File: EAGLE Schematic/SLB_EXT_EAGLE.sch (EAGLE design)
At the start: 706 parts, among them J1 16P_HEADER_SMD, J10 DB2EVC-3.81-4P-GN, J11 1803280, J12 KH-PCB-6P6C, J13 WJ15EDGK-3.81-2P, J14 KH-PCB-6P6C, J15 B4B-XH-A(LF)(SN), J17 WJ15EDGK-3.81-2P, J18 B3B-XH-A(LF)(SN), J19 DNI, J2 Phoenix Pluggable 3.81mm 3 way, J20 USB-C-Socket, J21 B3B-XH-A(LF)(SN), J3 Phoenix Pluggable 3.81mm 2 way, J4 B4B-XH-A(LF)(SN), J5 B4B-XH-A(LF)(SN), J6 B4B-XH-A(LF)(SN), J7 B4B-XH-A(LF)(SN), J8 B4B-XH-A(LF)(SN), J9 1803455, K1_TR1 TLP3109A, K1_TR2 TLP3109A, K2 VCF4-1000, P1 DB2EVC-3.81-2P-GN, P10 DB2ERC-5.08-2P-GN, P11 SHROUDED_BOX_HEADER_40, P12 HR911105A, P13 SHROUDED_BOX_HEADER_08, P14 SHROUDED_BOX_HEADER_08, P15 DNI, P16 SHROUDED_BOX_HEADER_08, P17 DB2EVC-3.81-7P-GN, P18_RL1 WJ15EDGK-3.81-2P, P18_RL2 WJ15EDGK-3.81-2P, P19 WJ15EDGK-3.81-2P, P2 DB2EVC-3.81-2P-GN, P20 SHROUDED_BOX_HEADER_08, P21_TR1 WJ15EDGK-3.81-2P, P21_TR2 WJ15EDGK-3.81-2P, P23 22284020, P24 1803329, P25 DNI, P26 DNI, P27 SHROUDED_BOX_HEADER_08, P28 DB2EVC-3.81-2P-GN, P3 DB2EVC-3.81-2P-GN, P4 DB2EVC-3.81-2P-GN, P5 Header 2, P6 WJ15EDGK-3.81-2P, P8 DNI, P9 DNI, Q1 WSF50P10, Q10_RL1 2N7002-7-F, Q10_RL2 2N7002-7-F, Q11 2N7002-7-F, Q12 2N7002-7-F, Q13 ST3422A, Q14 CSD19538Q3A, Q15 CSD19538Q3A, Q16 BSS123, Q17 BSS123, Q2_RL1 ST3422A, Q2_RL2 ST3422A, Q3 2N7002-7-F, Q4 2N7002-7-F, Q5 2N7002-7-F, Q6 2N7002-7-F, Q7 2N7002-7-F, Q8 2N7002-7-F, Q9_TR1 2N7002-7-F, Q9_TR2 2N7002-7-F, U1 SN74AHC1G86DBVR, U10 EL357N-G, U11 W5500, U12 CBMUD1201LAS8, U13 SN75176BDR, U14 ADUM1200ARZ-RL7, U15 EL357N-G, U16 TPS54331DR, U17 STM32F412VGT6STM32F412VGT6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

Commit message: Updated schematic
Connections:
- net HALT_PEN: now also U21.C
- net KPSTR_PEN: now also U22.C
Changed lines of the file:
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@@
 <label x="342.9" y="142.24" size="1.778" layer="95" rot="MR0"/>
+</segment>
+<segment>
+<pinref part="U21" gate="G$1" pin="C"/>
+<wire x1="124.46" y1="76.2" x2="142.24" y2="76.2" width="0.1524" layer="91"/>
+<label x="129.54" y="76.2" size="1.778" layer="95"/>
 </segment>
 </net>
@@
 <label x="342.9" y="139.7" size="1.778" layer="95" rot="MR0"/>
 </segment>
+<segment>
+<pinref part="U22" gate="G$1" pin="C"/>
+<wire x1="124.46" y1="38.1" x2="140.97" y2="38.1" width="0.1524" layer="91"/>
+<label x="127" y="38.1" size="1.778" layer="95"/>
+</segment>
 </net>

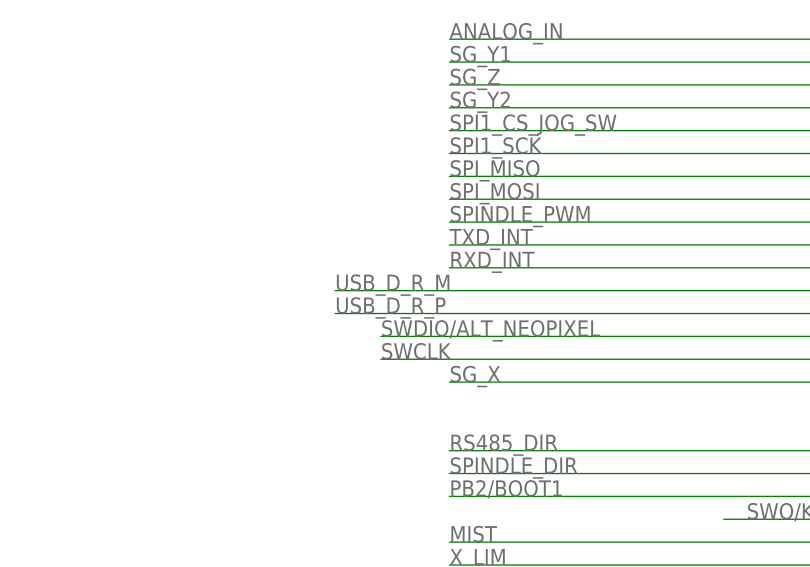
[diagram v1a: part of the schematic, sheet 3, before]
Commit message: Updated schematic (Incorrectly named NET)
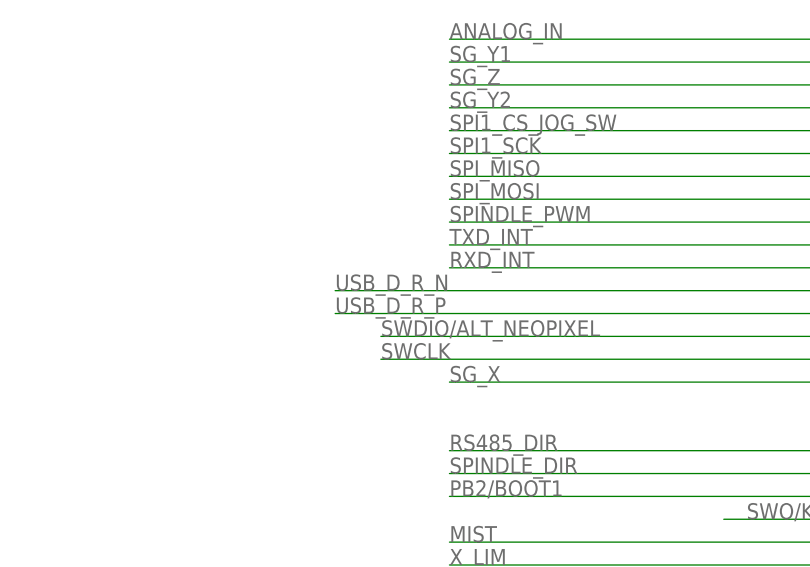
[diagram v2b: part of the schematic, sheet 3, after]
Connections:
- removed net USB_D_R_M: U17.PA11/OTG_FS_DM
- net USB_D_R_N: now also U17.PA11/OTG_FS_DM
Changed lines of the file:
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@@
 </busses>
 <nets>
-<net name="USB_D_R_M" class="0">
-<segment>
-<wire x1="132.08" y1="104.14" x2="76.2" y2="104.14" width="0.1524" layer="91"/>
-<label x="76.2" y="104.14" size="1.778" layer="95"/>
-<pinref part="U17" gate="G$1" pin="PA11/OTG_FS_DM"/>
-</segment>
-</net>
 <net name="STM_NRST" class="0">
 <segment>
@@
 <pinref part="R67" gate="G$1" pin="1"/>
 </segment>
-</net>
+<segment>
+<wire x1="132.08" y1="104.14" x2="76.2" y2="104.14" width="0.1524" layer="91"/>
+<label x="76.2" y="104.14" size="1.778" layer="95"/>
+<pinref part="U17" gate="G$1" pin="PA11/OTG_FS_DM"/>
+</segment>
+</net>

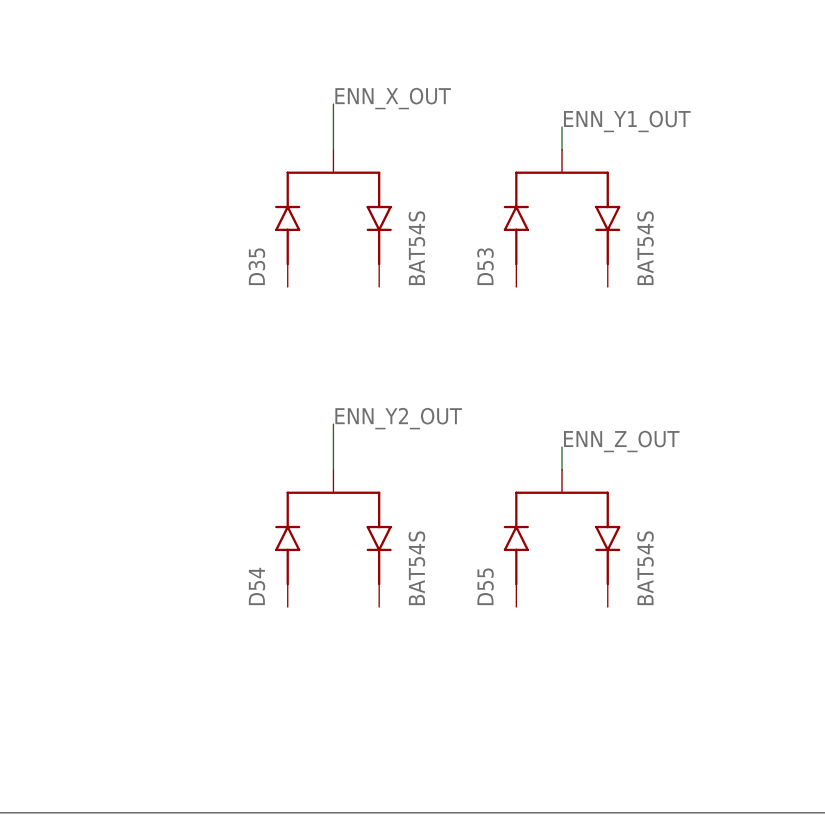
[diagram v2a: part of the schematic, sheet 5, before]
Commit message: Fix disconnected nets on BAT54S components
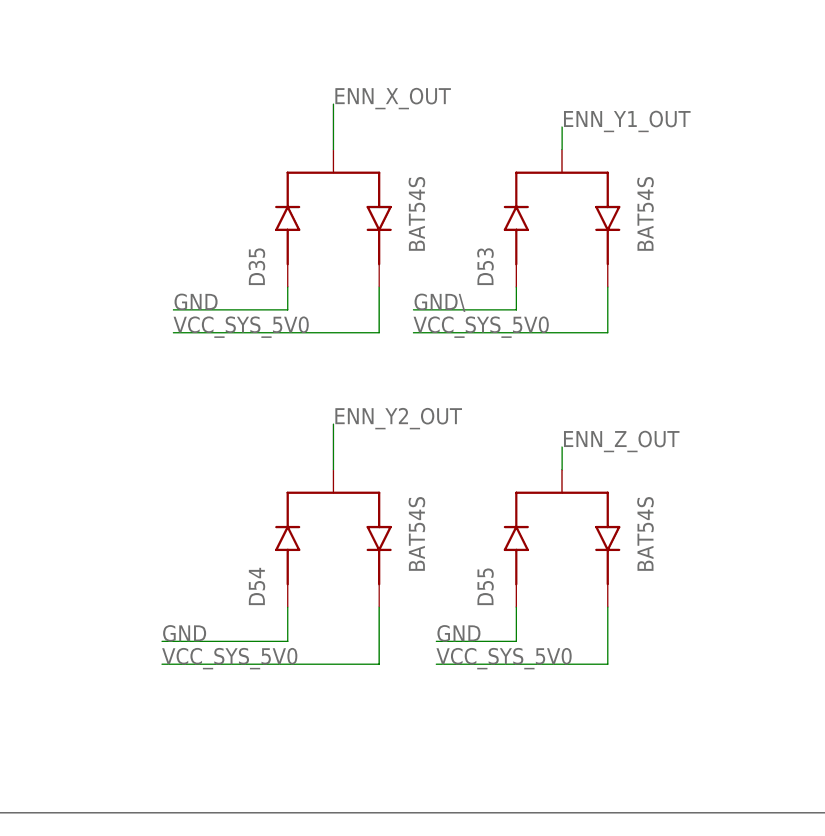
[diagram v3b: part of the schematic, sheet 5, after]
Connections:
- new net GND\: D53.1
- net GND: now also D35.1, D54.1, D55.1
- net VCC_SYS_5V0: now also D35.2, D53.2, D54.2, D55.2
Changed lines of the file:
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@@
 <instance part="D35" gate="G$1" x="304.8" y="180.34" smashed="yes" rot="R90">
 <attribute name="NAME" x="297.18" y="172.72" size="1.778" layer="95" rot="R90"/>
-<attribute name="VALUE" x="314.96" y="172.72" size="1.778" layer="96" rot="R90"/>
+<attribute name="VALUE" x="314.96" y="176.53" size="1.778" layer="96" rot="R90"/>
 </instance>
 <instance part="D53" gate="G$1" x="330.2" y="180.34" smashed="yes" rot="R90">
 <attribute name="NAME" x="322.58" y="172.72" size="1.778" layer="95" rot="R90"/>
-<attribute name="VALUE" x="340.36" y="172.72" size="1.778" layer="96" rot="R90"/>
+<attribute name="VALUE" x="340.36" y="176.53" size="1.778" layer="96" rot="R90"/>
 </instance>
 <instance part="D54" gate="G$1" x="304.8" y="144.78" smashed="yes" rot="R90">
 <attribute name="NAME" x="297.18" y="137.16" size="1.778" layer="95" rot="R90"/>
-<attribute name="VALUE" x="314.96" y="137.16" size="1.778" layer="96" rot="R90"/>
+<attribute name="VALUE" x="314.96" y="140.97" size="1.778" layer="96" rot="R90"/>
 </instance>
 <instance part="D55" gate="G$1" x="330.2" y="144.78" smashed="yes" rot="R90">
 <attribute name="NAME" x="322.58" y="137.16" size="1.778" layer="95" rot="R90"/>
-<attribute name="VALUE" x="340.36" y="137.16" size="1.778" layer="96" rot="R90"/>
+<attribute name="VALUE" x="340.36" y="140.97" size="1.778" layer="96" rot="R90"/>
 </instance>
 <instance part="U39" gate="G$1" x="124.46" y="55.88" smashed="yes" rot="MR0">
@@
 <wire x1="127" y1="144.78" x2="127" y2="137.16" width="0.1524" layer="91"/>
 </segment>
+<segment>
+<pinref part="D35" gate="G$1" pin="1"/>
+<wire x1="299.72" y1="172.72" x2="299.72" y2="170.18" width="0.1524" layer="91"/>
+<wire x1="299.72" y1="170.18" x2="287.02" y2="170.18" width="0.1524" layer="91"/>
+<label x="287.02" y="170.18" size="1.778" layer="95"/>
+</segment>
+<segment>
+<pinref part="D54" gate="G$1" pin="1"/>
+<wire x1="299.72" y1="137.16" x2="299.72" y2="133.35" width="0.1524" layer="91"/>
+<wire x1="299.72" y1="133.35" x2="285.75" y2="133.35" width="0.1524" layer="91"/>
+<label x="285.75" y="133.35" size="1.778" layer="95"/>
+</segment>
+<segment>
+<pinref part="D55" gate="G$1" pin="1"/>
+<wire x1="325.12" y1="137.16" x2="325.12" y2="133.35" width="0.1524" layer="91"/>
+<wire x1="325.12" y1="133.35" x2="316.23" y2="133.35" width="0.1524" layer="91"/>
+<label x="316.23" y="133.35" size="1.778" layer="95"/>
+</segment>
 </net>
 <net name="MCU_GND" class="0">
@@
 <wire x1="264.16" y1="43.18" x2="269.24" y2="43.18" width="0.1524" layer="91"/>
 <label x="266.7" y="43.18" size="1.778" layer="95"/>
+</segment>
+<segment>
+<pinref part="D54" gate="G$1" pin="2"/>
+<wire x1="309.88" y1="137.16" x2="309.88" y2="130.81" width="0.1524" layer="91"/>
+<wire x1="309.88" y1="130.81" x2="285.75" y2="130.81" width="0.1524" layer="91"/>
+<label x="285.75" y="130.81" size="1.778" layer="95"/>
+</segment>
+<segment>
+<pinref part="D55" gate="G$1" pin="2"/>
+<wire x1="335.28" y1="137.16" x2="335.28" y2="130.81" width="0.1524" layer="91"/>
+<wire x1="335.28" y1="130.81" x2="316.23" y2="130.81" width="0.1524" layer="91"/>
+<label x="316.23" y="130.81" size="1.778" layer="95"/>
+</segment>
+<segment>
+<pinref part="D35" gate="G$1" pin="2"/>
+<wire x1="309.88" y1="172.72" x2="309.88" y2="167.64" width="0.1524" layer="91"/>
+<wire x1="309.88" y1="167.64" x2="287.02" y2="167.64" width="0.1524" layer="91"/>
+<label x="287.02" y="167.64" size="1.778" layer="95"/>
+</segment>
+<segment>
+<pinref part="D53" gate="G$1" pin="2"/>
+<wire x1="335.28" y1="172.72" x2="335.28" y2="167.64" width="0.1524" layer="91"/>
+<wire x1="335.28" y1="167.64" x2="313.69" y2="167.64" width="0.1524" layer="91"/>
+<label x="313.69" y="167.64" size="1.778" layer="95"/>
 </segment>
 </net>
@@
 </segment>
 </net>
+<net name="GND\" class="0">
+<segment>
+<pinref part="D53" gate="G$1" pin="1"/>
+<wire x1="325.12" y1="172.72" x2="325.12" y2="170.18" width="0.1524" layer="91"/>
+<wire x1="325.12" y1="170.18" x2="313.69" y2="170.18" width="0.1524" layer="91"/>
+<label x="313.69" y="170.18" size="1.778" layer="95"/>
+</segment>
+</net>
